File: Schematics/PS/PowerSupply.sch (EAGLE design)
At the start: 81 parts, among them IC1 LM317MABDT, IC2 LM337, T1 IRFP240, T2 IRFP240

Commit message: making a commit before i start new schematic
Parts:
- removed C19: 15,000uF, Amplifier_Parts:LNR1K153MSE
- removed C25: 1uF, rcl:CPOL-EUE2.5-6
- removed L1: CHOKE, Amplifier_Parts:CHOKE
- added L2: CHOKE, Amplifier_Parts:CHOKE
- C13: value 15,000uF -> 1uF; device Amplifier_Parts:LNR1K153MSE -> rcl:C-EU102-064X133
- C3: device rcl:C-EU102-064X133 -> rcl:CPOL-EUE2.5-6
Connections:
- removed net N$16: L1.W2A, U$2.S3
- removed net PE: C3.2
- removed net V-: C25.-
- new net EGND: C28.1, U$2.S2
- new net SOMENET: C17.1, L2.PASS1, R10.1, R11.1, R9.1, U$1.COM
- net GND: now also C13.2, C4.-; no longer C17.1, L1.W2E, R10.1, R11.1, R9.1, U$1.COM
- net N$10: now also C13.1; no longer C3.1
- net N$12: now also U$4.P$2; no longer C28.1
- net N$15: now also L2.PASS12, U$2.S1; no longer L1.W1A, U$2.S5
- net N$2: now also L2.PASS22, U$2.S3; no longer U$2.S1, U$4.P$1
- net N$4: now also L2.PASS2; no longer L1.W1E
- net N$5: now also U$2.S5, U$4.P$1; no longer U$2.S2, U$4.P$2
- net SGND: now also C3.+; no longer C13.+, C19.-, C25.+
- net V15-: now also C3.-
- net VAC-40: no longer D10.NC@2
- net VCC: no longer C19.+
- net VEE: no longer C13.-
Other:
- note added: "removed large caps to save space"
- moved on the sheet: C28, C9, R17, U$2

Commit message: fixed PS issue
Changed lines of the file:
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@@
 <part name="D10" library="Amplifier_Parts" deviceset="VS-ETL1506-M3" device=""/>
 <part name="PE15" library="supply1" deviceset="PE" device=""/>
+<part name="P-1" library="supply1" deviceset="V-" device=""/>
 <part name="C3" library="rcl" deviceset="CPOL-EU" device="E2.5-6" value="1uF"/>
-<part name="P-1" library="supply1" deviceset="V-" device=""/>
 <part name="C13" library="rcl" deviceset="C-EU" device="102-064X133" value="1uF"/>
+<part name="PE4" library="supply1" deviceset="PE" device=""/>
 </parts>
 <sheets>
@@
 <instance part="D10" gate="G$1" x="76.2" y="12.7"/>
 <instance part="PE15" gate="M" x="30.48" y="-38.1"/>
+<instance part="P-1" gate="1" x="172.72" y="-76.2"/>
 <instance part="C3" gate="G$1" x="172.72" y="-63.5" smashed="yes">
 <attribute name="NAME" x="174.244" y="-63.119" size="1.778" layer="95"/>
 <attribute name="VALUE" x="174.244" y="-60.579" size="1.778" layer="96"/>
 </instance>
-<instance part="P-1" gate="1" x="172.72" y="-76.2"/>
 <instance part="C13" gate="G$1" x="17.78" y="-5.08"/>
+<instance part="PE4" gate="M" x="20.32" y="-12.7"/>
 </instances>
 <busses>
@@
 <pinref part="U$1" gate="G$1" pin="COIL+"/>
 <pinref part="PE8" gate="M" pin="PE"/>
-<wire x1="30.48" y1="0" x2="35.56" y2="0" width="0.1524" layer="91"/>
-<wire x1="35.56" y1="0" x2="35.56" y2="-10.16" width="0.1524" layer="91"/>
-<wire x1="35.56" y1="-10.16" x2="17.78" y2="-10.16" width="0.1524" layer="91"/>
-<pinref part="C13" gate="G$1" pin="2"/>
 </segment>
 <segment>
@@
 <pinref part="C4" gate="G$1" pin="-"/>
 <pinref part="PE9" gate="M" pin="PE"/>
+</segment>
+<segment>
+<pinref part="C13" gate="G$1" pin="2"/>
+<pinref part="PE4" gate="M" pin="PE"/>
+<wire x1="20.32" y1="-10.16" x2="17.78" y2="-10.16" width="0.1524" layer="91"/>
 </segment>
 </net>
@@
 <junction x="165.1" y="-50.8"/>
 <junction x="134.62" y="-50.8"/>
-<wire x1="172.72" y1="-50.8" x2="172.72" y2="-60.96" width="0.1524" layer="91"/>
-<junction x="172.72" y="-50.8"/>
 <pinref part="C14" gate="G$1" pin="-"/>
 <pinref part="C3" gate="G$1" pin="+"/>
+<wire x1="172.72" y1="-50.8" x2="172.72" y2="-60.96" width="0.1524" layer="91"/>
 </segment>
 </net>
@@
 </segment>
 <segment>
-<wire x1="172.72" y1="-68.58" x2="172.72" y2="-71.12" width="0.1524" layer="91"/>
 <pinref part="IC2" gate="G$1" pin="OUT"/>
 <pinref part="R22" gate="G$1" pin="1"/>
@@
 <wire x1="165.1" y1="-71.12" x2="172.72" y2="-71.12" width="0.1524" layer="91"/>
 <junction x="165.1" y="-71.12"/>
-<junction x="172.72" y="-71.12"/>
+<pinref part="P-1" gate="1" pin="V-"/>
 <pinref part="C3" gate="G$1" pin="-"/>
-<pinref part="P-1" gate="1" pin="V-"/>
-</segment>
-</net>
+<wire x1="172.72" y1="-71.12" x2="172.72" y2="-68.58" width="0.1524" layer="91"/>
+</segment>
+</net>

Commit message: finished powersuply :) updated parts on hand
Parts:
- C28: device rcl:C-EU102-064X133 -> rcl:C-EUC0805K
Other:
- moved on the sheet: C28
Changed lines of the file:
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@@
 <part name="C14" library="rcl" deviceset="CPOL-EU" device="E2.5-6" value="1uF"/>
 <part name="C26" library="resistor" deviceset="C-EU" device="025-025X050" value="1uF"/>
-<part name="C28" library="rcl" deviceset="C-EU" device="102-064X133" value="1nF"/>
+<part name="C28" library="rcl" deviceset="C-EU" device="C0805K" value="1nF"/>
 <part name="D19" library="Amplifier_Parts" deviceset="1N4004" device=""/>
 <part name="PE10" library="supply1" deviceset="PE" device=""/>
@@
 <instance part="C1" gate="G$1" x="78.74" y="50.8" rot="R180"/>
 <instance part="U$6" gate="G$1" x="27.94" y="76.2"/>
-<instance part="PE7" gate="M" x="-5.08" y="66.04" rot="R90"/>
+<instance part="PE7" gate="M" x="-10.16" y="66.04" rot="R90"/>
 <instance part="C4" gate="G$1" x="71.12" y="66.04" smashed="yes">
 <attribute name="NAME" x="72.644" y="66.421" size="1.778" layer="95"/>
@@
 <attribute name="VALUE" x="157.099" y="42.164" size="1.778" layer="96" rot="R90"/>
 </instance>
-<instance part="C28" gate="G$1" x="-15.24" y="66.04" smashed="yes" rot="R90">
-<attribute name="NAME" x="-11.684" y="63.119" size="1.778" layer="95" rot="R180"/>
+<instance part="C28" gate="G$1" x="-17.78" y="66.04" smashed="yes" rot="R90">
+<attribute name="NAME" x="-16.764" y="63.119" size="1.778" layer="95" rot="R180"/>
+<attribute name="VALUE" x="-16.764" y="70.739" size="1.778" layer="96" rot="R180"/>
 </instance>
 <instance part="D19" gate="G$1" x="104.14" y="81.28" smashed="yes">
@@
 <pinref part="PE7" gate="M" pin="PE"/>
 <pinref part="C28" gate="G$1" pin="2"/>
-<wire x1="-7.62" y1="66.04" x2="-10.16" y2="66.04" width="0.1524" layer="91"/>
 </segment>
 <segment>
@@
 <pinref part="C3" gate="G$1" pin="+"/>
 <wire x1="172.72" y1="-50.8" x2="172.72" y2="-60.96" width="0.1524" layer="91"/>
+<junction x="172.72" y="-50.8"/>
 </segment>
 </net>
@@
 <pinref part="U$2" gate="G$1" pin="S2"/>
 <pinref part="C28" gate="G$1" pin="1"/>
-<wire x1="-20.32" y1="66.04" x2="-17.78" y2="66.04" width="0.1524" layer="91"/>
-</segment>
-</net>
+</segment>
+</net>

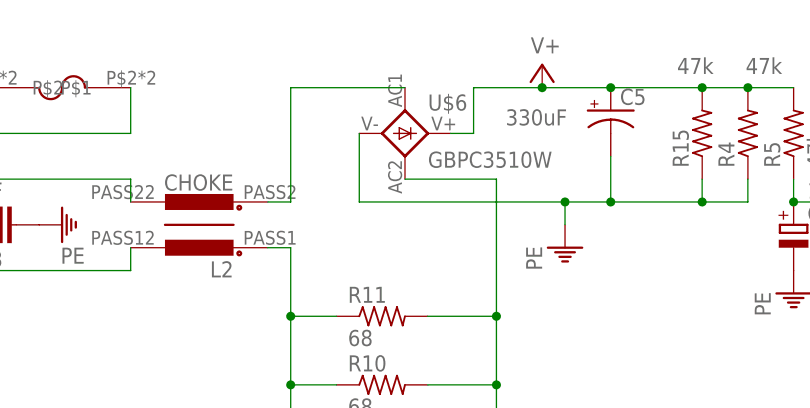
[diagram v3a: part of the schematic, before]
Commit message: fixed PS layout (changed rectifier footprint)
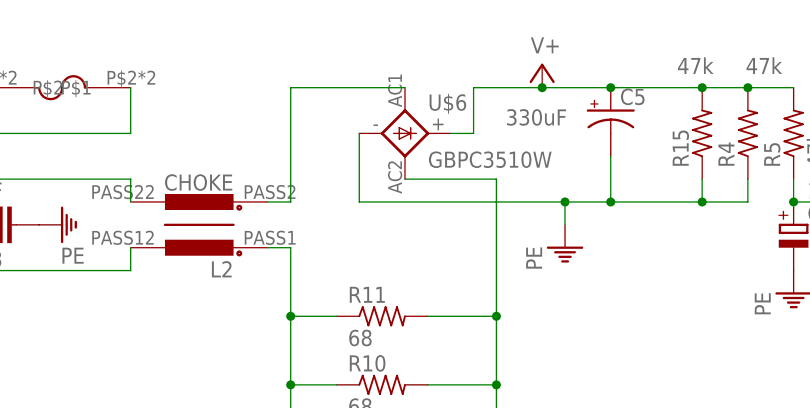
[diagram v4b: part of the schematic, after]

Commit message: updates to PS layout
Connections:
- net N$15 renamed LINE
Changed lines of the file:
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@@
 </segment>
 </net>
-<net name="N$15" class="0">
+<net name="LINE" class="0">
 <segment>
 <pinref part="L2" gate="G$1" pin="PASS12"/>

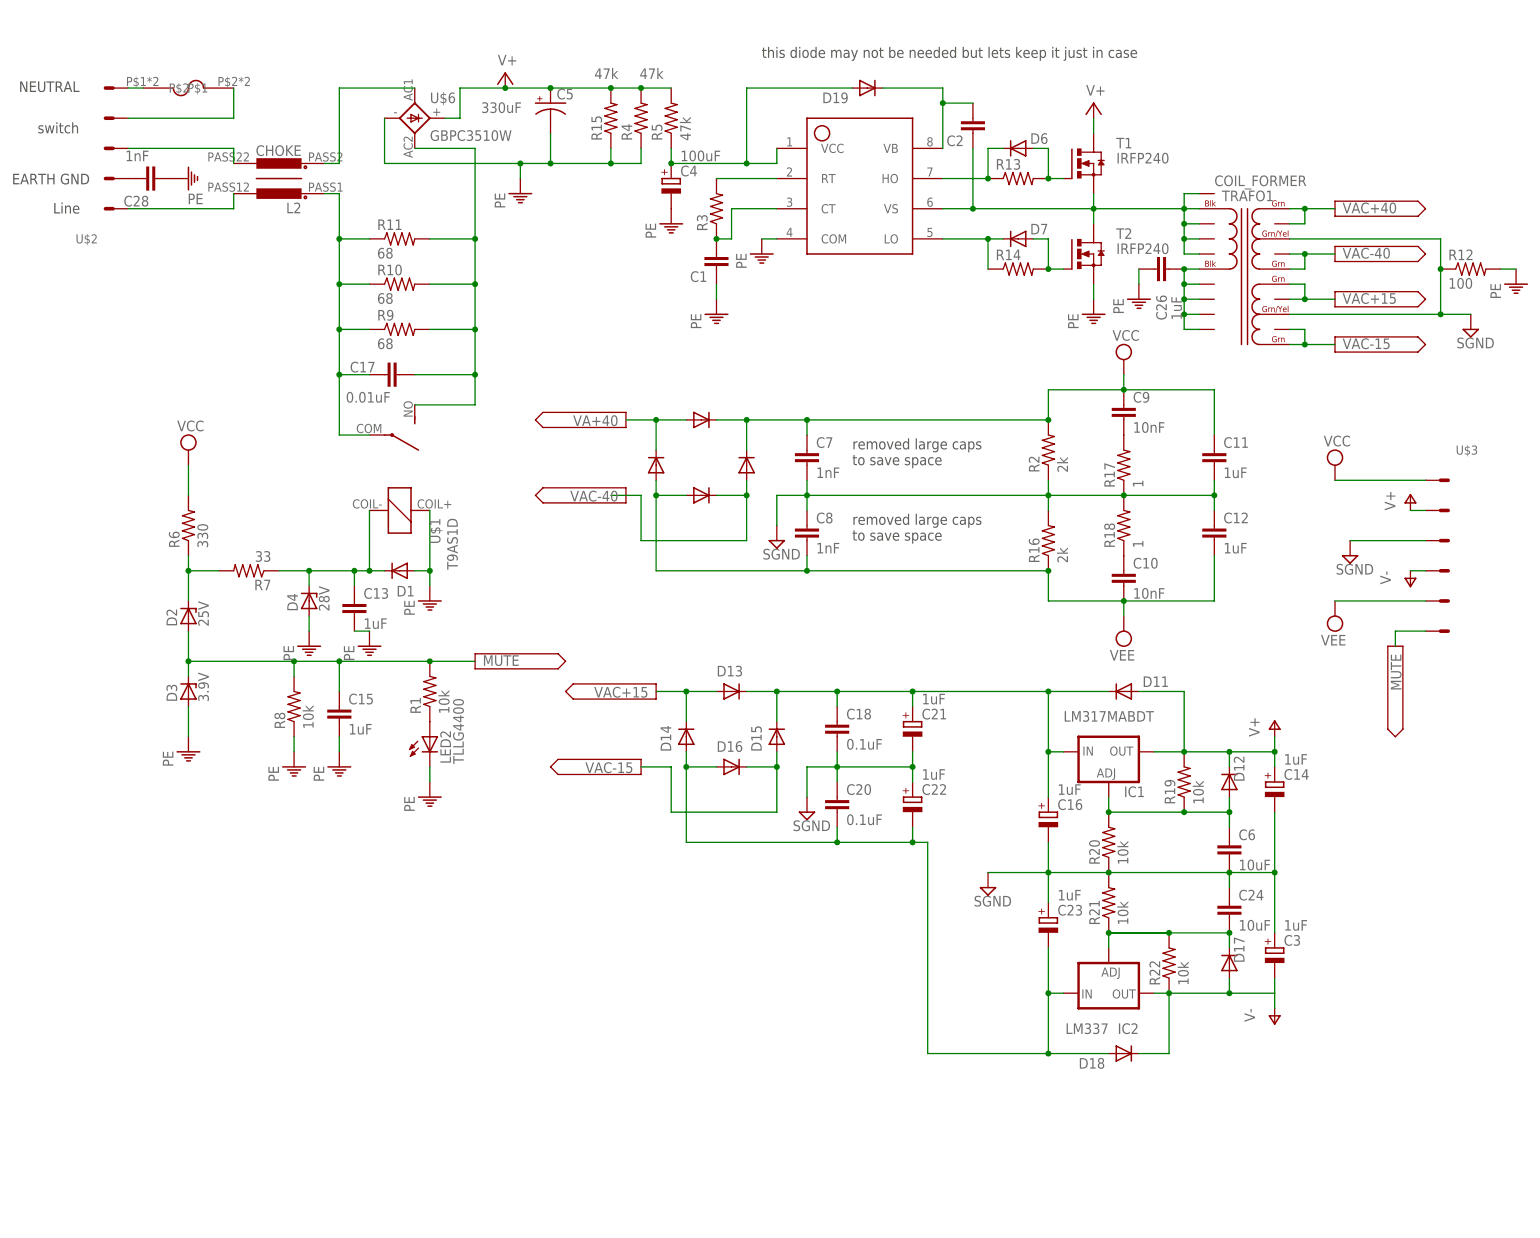
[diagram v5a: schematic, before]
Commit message: added names to input and output traces on filter board
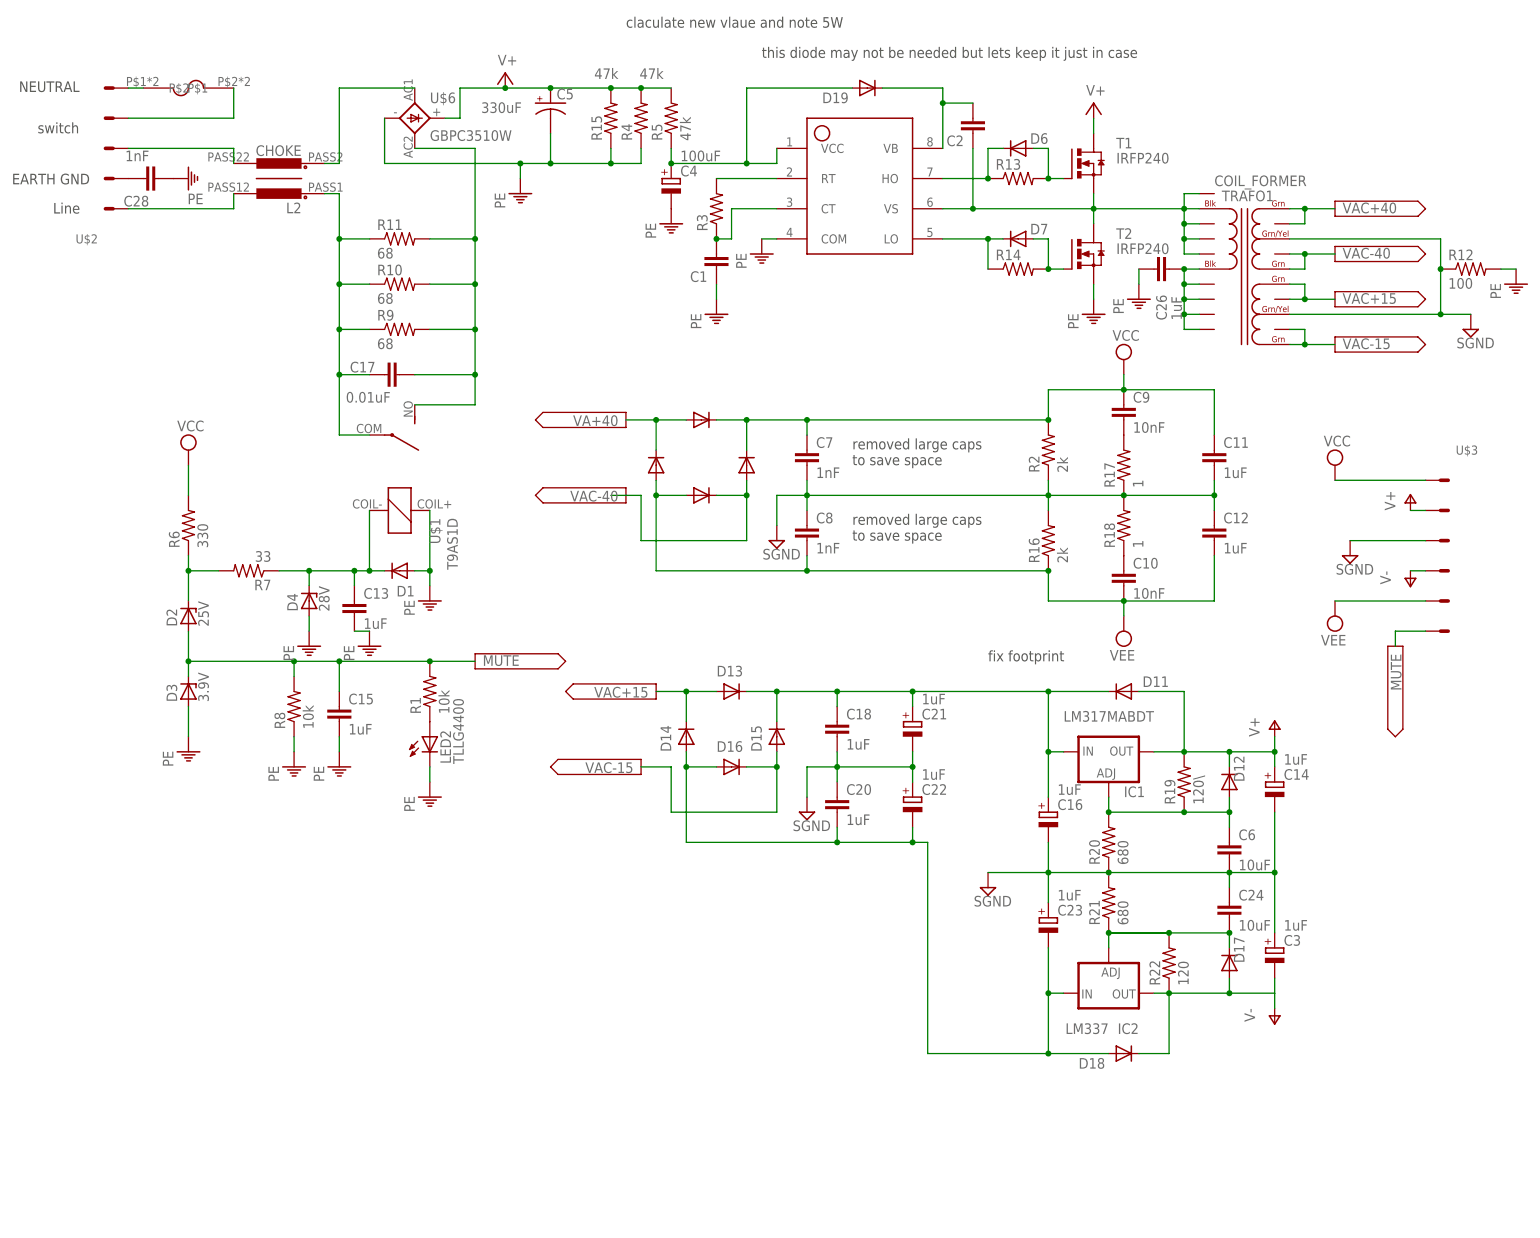
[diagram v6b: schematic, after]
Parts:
- C18, C20: value 0.1uF -> 1uF
- R19: value 10k -> 120\
- R20, R21: value 10k -> 680
- R22: value 10k -> 120
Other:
- note added: "claculate new vlaue and note 5W"
- note added: "fix footprint"
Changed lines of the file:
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@@
 <part name="D11" library="Amplifier_Parts" deviceset="1N4004" device=""/>
 <part name="D12" library="Amplifier_Parts" deviceset="1N4004" device=""/>
-<part name="R19" library="rcl" deviceset="R-US_" device="0204/2V" value="10k"/>
-<part name="R20" library="rcl" deviceset="R-US_" device="0204/2V" value="10k"/>
+<part name="R19" library="rcl" deviceset="R-US_" device="0204/2V" value="120\"/>
+<part name="R20" library="rcl" deviceset="R-US_" device="0204/2V" value="680"/>
 <part name="C6" library="resistor" deviceset="C-EU" device="025-025X050" value="10uF"/>
 <part name="SGND2" library="supply2" deviceset="GND5" device="" value="SGND"/>
-<part name="C18" library="rcl" deviceset="C-EU" device="102-064X133" value="0.1uF"/>
-<part name="C20" library="rcl" deviceset="C-EU" device="102-064X133" value="0.1uF"/>
+<part name="C18" library="rcl" deviceset="C-EU" device="102-064X133" value="1uF"/>
+<part name="C20" library="rcl" deviceset="C-EU" device="102-064X133" value="1uF"/>
 <part name="D13" library="Amplifier_Parts" deviceset="1N4004" device=""/>
 <part name="D14" library="Amplifier_Parts" deviceset="1N4004" device=""/>
@@
 <part name="D16" library="Amplifier_Parts" deviceset="1N4004" device=""/>
 <part name="IC2" library="Amplifier_Parts" deviceset="LM337" device=""/>
-<part name="R21" library="rcl" deviceset="R-US_" device="0204/2V" value="10k"/>
+<part name="R21" library="rcl" deviceset="R-US_" device="0204/2V" value="680"/>
 <part name="C16" library="rcl" deviceset="CPOL-EU" device="E2.5-6" value="1uF"/>
 <part name="C23" library="rcl" deviceset="CPOL-EU" device="E2.5-6" value="1uF"/>
-<part name="R22" library="rcl" deviceset="R-US_" device="0204/2V" value="10k"/>
+<part name="R22" library="rcl" deviceset="R-US_" device="0204/2V" value="120"/>
 <part name="D17" library="Amplifier_Parts" deviceset="1N4004" device=""/>
 <part name="C24" library="resistor" deviceset="C-EU" device="025-025X050" value="10uF"/>
@@
 <text x="101.6" y="5.08" size="1.778" layer="97">removed large caps
 to save space</text>
+<text x="63.5" y="91.44" size="1.778" layer="97">claculate new vlaue and note 5W</text>
+<text x="124.46" y="-15.24" size="1.778" layer="97">fix footprint</text>
 </plain>
 <instances>

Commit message: fixed power supply board
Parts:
- added R23, R24: (no value), pot:TRIM_EU-B25P
- added R25: 390, rcl:R-US_0204/2V
- C1: value (none) -> 390pF
- R5: value 47k -> 23.5k
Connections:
- new net N$15: R20.1, R23.E, R23.S
- new net N$16: C13.1, D1.C, D4.C, R25.1, R7.1
- new net N$23: R21.2, R24.A
- net GND: no longer LED2.C
- net N$10: now also R25.2; no longer C13.1, D1.C, D4.C, R7.1
- net SGND: now also LED2.C, R23.A, R24.E, R24.S; no longer R20.1, R21.2
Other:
- note added: "2X"
- note added: "5W"
- note added: "stack 2k resistors"
- note removed: "claculate new vlaue and note 5W"
- note removed: "fix footprint"
- note removed: "this diode may not be needed but lets keep it just in case"
- moved on the sheet: C23, C24, C3, D17, D18, D4, IC2, R21, R22, R7
